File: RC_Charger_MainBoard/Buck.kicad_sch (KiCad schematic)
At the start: 14 parts, among them U5 TPS54560BDDA

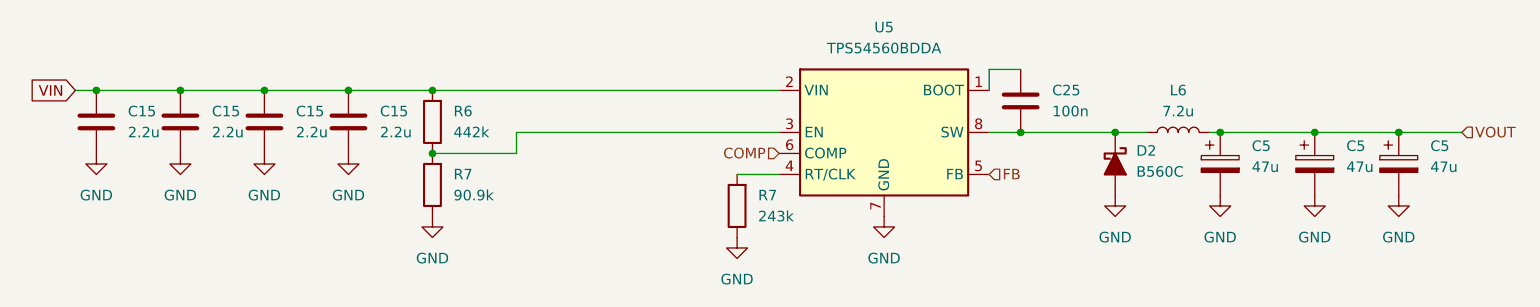
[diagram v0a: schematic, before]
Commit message: Change components for costdown
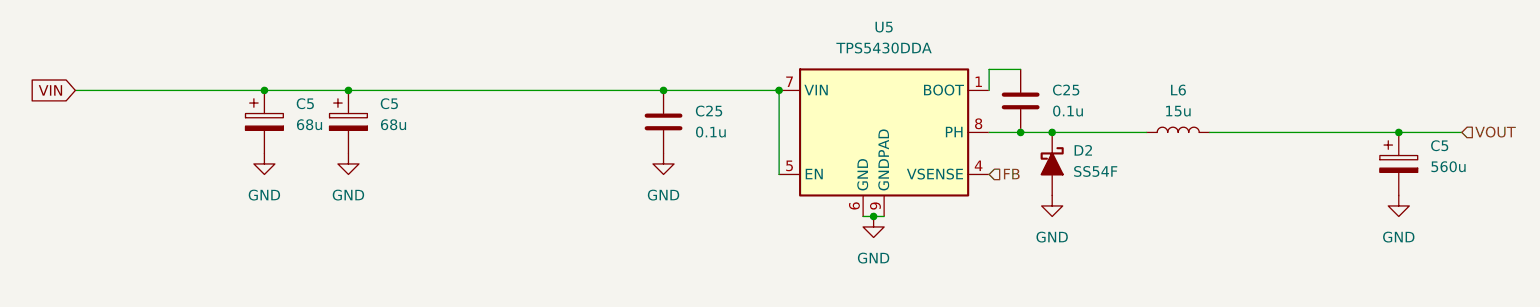
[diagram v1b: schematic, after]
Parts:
- removed C15 (x4): 2.2u, Capacitor_SMD:C_0805_2012Metric, symbol Device:C
- removed C5 (x2): 47u, Capacitor_SMD:CP_Elec_5x5.8, symbol Device:C_Polarized
- removed D2: B560C, Diode_SMD:D_SMC, symbol PCM_Diode_Schottky_AKL:B560C
- removed R6: 442k, Resistor_SMD:R_0603_1608Metric, symbol Device:R
- removed R7: 243k, Resistor_SMD:R_0603_1608Metric, symbol Device:R
- removed R7: 90.9k, Resistor_SMD:R_0603_1608Metric, symbol Device:R
- removed U5: TPS54560BDDA, Package_SO:Texas_R-PDSO-G8_EP2.95x4.9mm_Mask2.4x3.1mm_ThermalVias, symbol Regulator_Switching:TPS54560BDDA
- added C25: 0.1u, Capacitor_SMD:C_0603_1608Metric, symbol Device:C
- added C5 (x2): 68u, Capacitor_SMD:CP_Elec_6.3x7.7, symbol Device:C_Polarized
- added D2: SS54F, Diode_SMD:D_SMA, symbol PCM_Diode_Schottky_AKL:SS54F
- added U5: TPS5430DDA, Package_SO:Texas_R-PDSO-G8_EP2.95x4.9mm_Mask2.4x3.1mm_ThermalVias, symbol Regulator_Switching:TPS5430DDA
- C25: value 100n -> 0.1u
- C5: value 47u -> 560u; footprint Capacitor_SMD:CP_Elec_5x5.8 -> Capacitor_SMD:CP_Elec_10x10
- L6: value 7.2u -> 15u; footprint Inductor_SMD:L_Bourns_SRP1038C_10.0x10.0mm -> Inductor_SMD:L_Bourns_SRR1260
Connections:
- net FB: now also U5.4 (VSENSE)
- net GND: now also C25.2, C5.2, C5.2, D2.2 (A), U5.6 (GND), U5.9 (GNDPAD)
- net VIN: now also C25.1, C5.1, C5.1, U5.5 (EN), U5.7 (VIN)
- net at C25.1: now also U5.1 (BOOT)
- net at C25.2, L6.1: now also D2.1 (K), U5.8 (PH)
